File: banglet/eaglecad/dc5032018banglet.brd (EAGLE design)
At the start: 39.8 x 22.6 mm, 39 parts, among them Q3 DMG3415U-7, U2 AP2112(3.3V), U3 MCP73831T-2ACI/OT, U4 CP2104, X1 32.768, X2 JSTPH, X4 20329

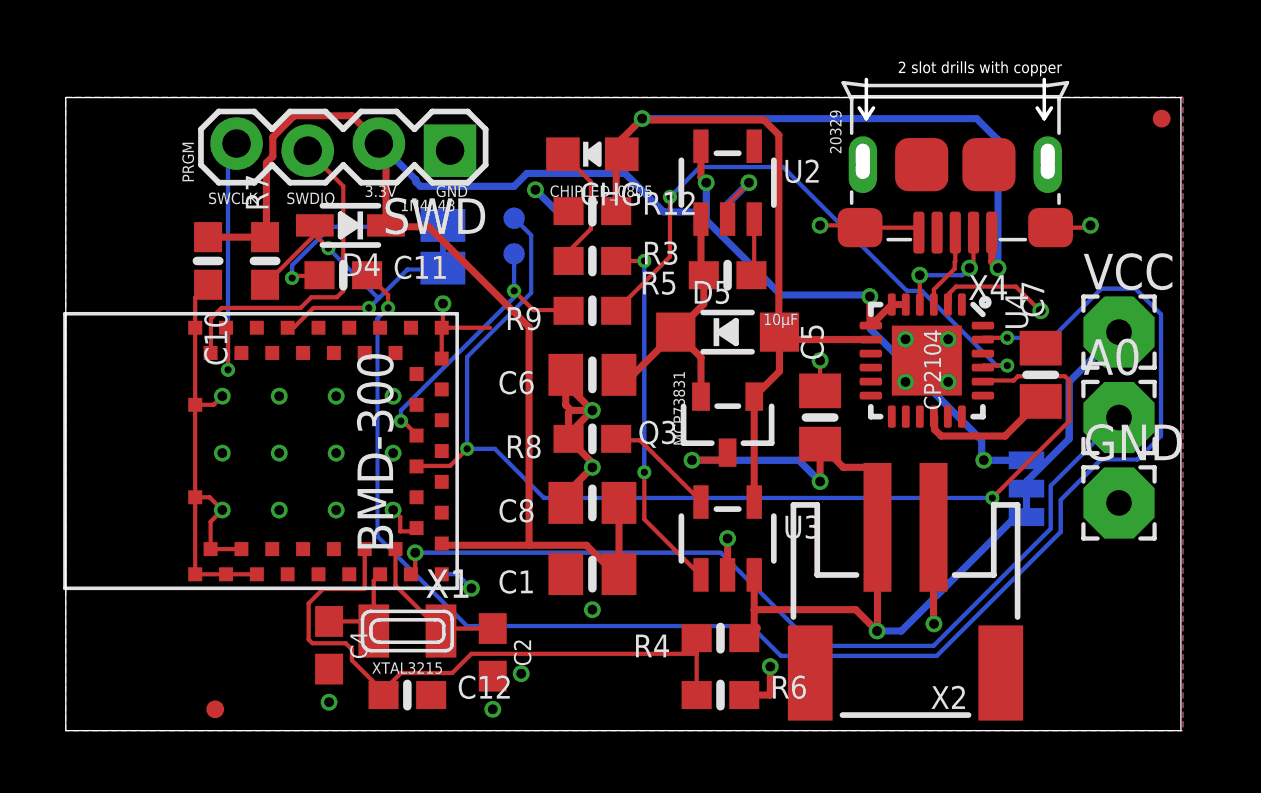
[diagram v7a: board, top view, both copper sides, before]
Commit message: move .1uF to next to nrf
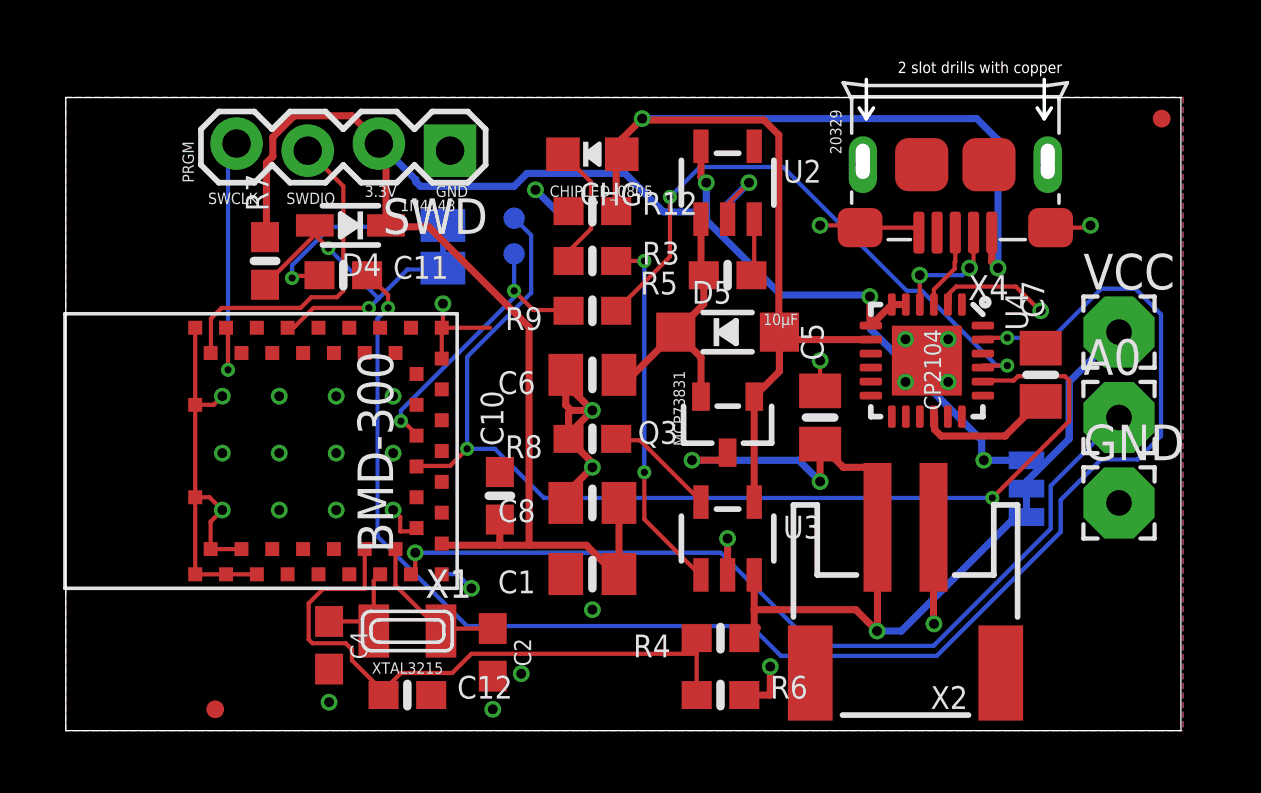
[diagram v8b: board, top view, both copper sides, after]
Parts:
- moved C10 13.4 mm to (15.5, 39.6), turned to 90 degrees
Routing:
- net GND: track 55.4 -> 53.7 mm
- net 3.3V: track 71.6 -> 70.4 mm
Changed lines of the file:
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@@
 <element name="A0" library="wirepad" library_urn="urn:adsk.eagle:library:412" package="2,54/0,9" value="WIREPAD2,54/0,9" x="37.592" y="42.418"/>
 <element name="C1" library="microbuilder" package="0805-NO" value="10uf" x="18.796" y="36.83" rot="R180"/>
-<element name="C10" library="microbuilder" package="0603-NO" value="0.1uF" x="5.08" y="48.006" rot="R270"/>
+<element name="C10" library="microbuilder" package="0603-NO" value="0.1uF" x="15.494" y="39.624" rot="R90"/>
 <element name="C11" library="microbuilder" package="0603-NO" value="0.1uF" x="9.906" y="47.498"/>
 <element name="C12" library="microbuilder" package="0603-NO" value="1nF" x="12.192" y="32.512"/>
@@
 <via x="26.924" y="44.45" extent="1-16" drill="0.35"/>
 <wire x1="15.142" y1="45.622" x2="13.42" y2="45.622" width="0.1524" layer="1"/>
-<wire x1="4.62" y1="45.622" x2="4.62" y2="46.696" width="0.1524" layer="1"/>
-<wire x1="4.62" y1="46.696" x2="5.08" y2="47.156" width="0.1524" layer="1"/>
 <wire x1="17.846" y1="36.83" x2="17.846" y2="36.51" width="0.254" layer="1"/>
 <wire x1="17.846" y1="39.37" x2="17.846" y2="39.69" width="0.254" layer="1"/>
@@
 <wire x1="22.672" y1="50.988" x2="22.86" y2="50.8" width="0.254" layer="1"/>
 <via x="22.86" y="50.8" extent="1-16" drill="0.35"/>
-<wire x1="7.112" y1="48.856" x2="5.08" y2="48.856" width="0.254" layer="1"/>
 <wire x1="11.43" y1="49.276" x2="11.43" y2="51.943" width="0.254" layer="1"/>
 <wire x1="11.43" y1="51.943" x2="11.176" y2="52.197" width="0.254" layer="1"/>
@@
 <wire x1="13.4826" y1="37.8594" x2="13.42" y2="37.922" width="0.254" layer="1"/>
 <wire x1="18.58173125" y1="37.8594" x2="16.5354" y2="37.8594" width="0.254" layer="1"/>
-<wire x1="16.5354" y1="37.8594" x2="13.4826" y2="37.8594" width="0.254" layer="1"/>
+<wire x1="16.5354" y1="37.8594" x2="15.494" y2="37.8594" width="0.254" layer="1"/>
+<wire x1="15.494" y1="37.8594" x2="13.4826" y2="37.8594" width="0.254" layer="1"/>
 <wire x1="7.1628" y1="51.5112" x2="7.1628" y2="48.9204" width="0.254" layer="1"/>
 <wire x1="7.3914" y1="51.7398" x2="7.1628" y2="51.5112" width="0.254" layer="1"/>
@@
 <wire x1="11.5062" y1="49.2252" x2="12.954" y2="49.2252" width="0.254" layer="1"/>
 <wire x1="11.5062" y1="49.2252" x2="11.43" y2="49.276" width="0.254" layer="1"/>
+<wire x1="15.494" y1="38.774" x2="15.494" y2="37.8594" width="0.254" layer="1"/>
 </signal>
 <signal name="VBUS" class="1">
